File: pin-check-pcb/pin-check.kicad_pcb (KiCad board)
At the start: 2 copper layers, 76.2 x 53.3 mm, 59 parts, among them J1 AVR-ISP-6, J2 SJ-43514, P1 USB_C_Receptacle_USB2.0, SW1 MX-NoLED, SW2 MX-NoLED, SW3 MX-NoLED, SW4 MX-NoLED, SW7 Reset, SW8 Boot, U1 ATmega328P-PU, Y1 16MHz

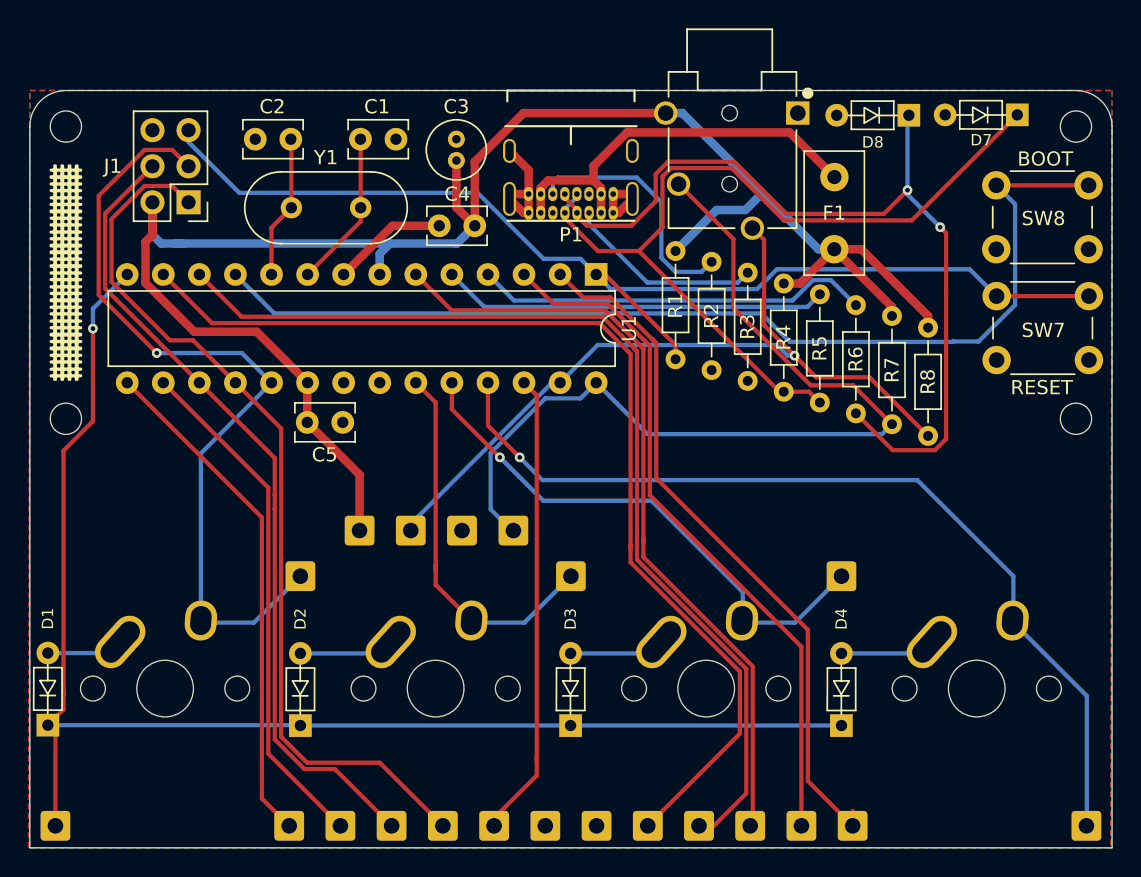
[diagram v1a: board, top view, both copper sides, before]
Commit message: buttons on top
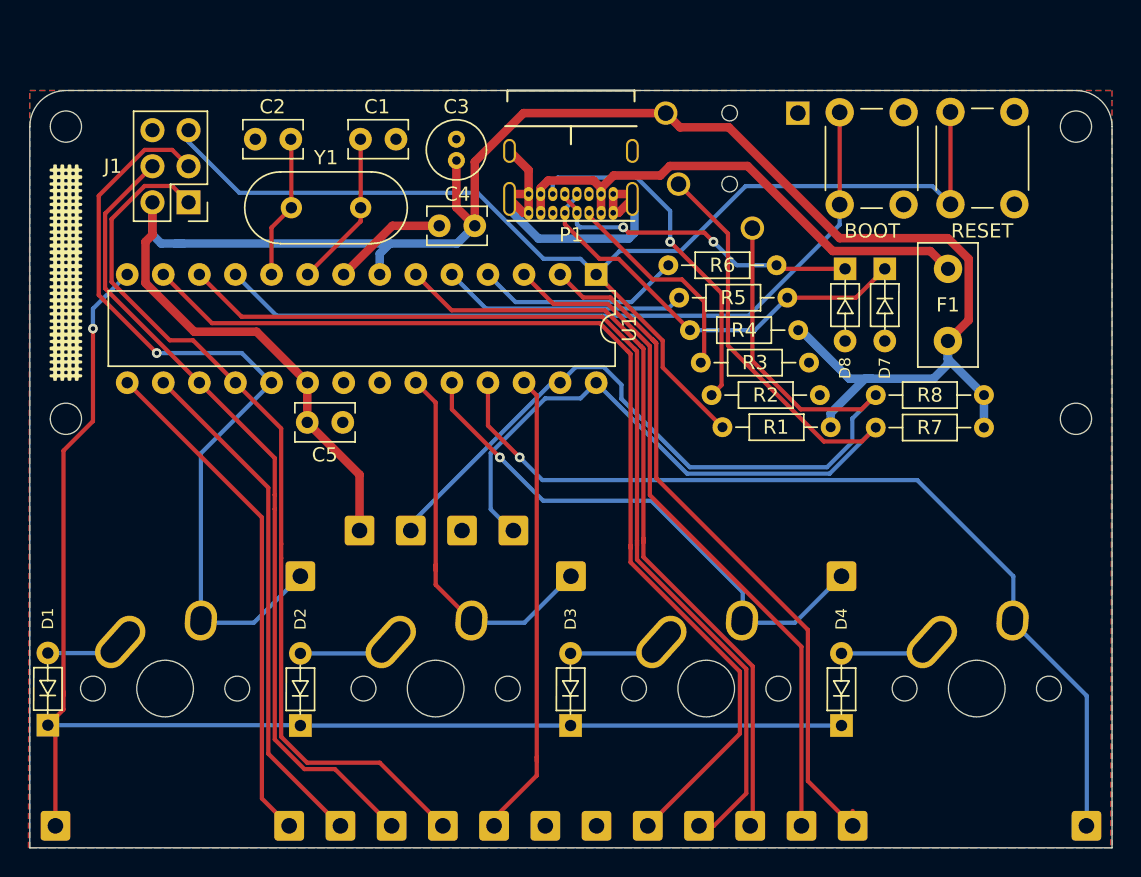
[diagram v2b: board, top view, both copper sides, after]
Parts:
- moved R1 16.5 mm to (167.2, 88.1), turned to 180 degrees
- moved D7 14.3 mm to (171.0, 75.7), turned to 270 degrees
- moved R6 11.8 mm to (163.4, 76.7), turned to 180 degrees
- moved D8 11.1 mm to (168.2, 75.7), turned to 270 degrees
- moved SW8 11.1 mm to (167.8, 72.4), turned to 90 degrees
- moved F1 10.3 mm to (175.4, 82.0)
- moved R7 10.2 mm to (178.0, 88.1), turned to 180 degrees
- moved R5 9.91 mm to (156.5, 79.0), turned to 0 degrees
- moved R2 9.38 mm to (158.8, 85.8), turned to 0 degrees
- moved SW7 7.24 mm to (175.6, 72.4), turned to 90 degrees
- moved R3 7.14 mm to (158.0, 83.5), turned to 0 degrees
- moved R8 6.17 mm to (178.0, 85.8), turned to 180 degrees
- moved R4 3.44 mm to (164.9, 81.2), turned to 180 degrees
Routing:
- net Net-(D8-Pad1): track 63.4 -> 22.9 mm
- net Net-(D7-Pad1): track 61.9 -> 30.2 mm
- net /Boot: track 73.7 -> 54.6 mm
- net GND: track 20.9 -> 35.8 mm
- net +5V: track 128.4 -> 142.5 mm
- net /D+: track 28.0 -> 14.6 mm
- net /D-: track 27.2 -> 17.3 mm
- net /SDA: track 54.9 -> 63.6 mm, vias 1 -> 0
- net Net-(F1-Pad2): track 28.5 -> 36.7 mm
- net Net-(P1-PadB5): track 17.5 -> 24.9 mm, vias 0 -> 1
- net /Reset: track 79.4 -> 83.9 mm
- net /SCL: track 63.1 -> 65.7 mm
- net Net-(P1-PadA5): track 14.5 -> 15.8 mm

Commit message: some changes
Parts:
- removed the H18 at (134.0, 95.3)
- added H22: Pad, Connector_Wire:SolderWire-0.5sqmm_1x01_D0.9mm_OD2.1mm, B.Cu at (182.9, 95.3)
- added H9: Pad, Connector_Wire:SolderWire-0.5sqmm_1x01_D0.9mm_OD2.1mm, B.Cu at (157.9, 116.1)
- moved H19 34.5 mm to (172.1, 95.3)
- moved H20 34.5 mm to (175.7, 95.3)
- moved H21 34.5 mm to (179.3, 95.3)
- moved H10 3.61 mm to (154.3, 116.1)
- moved H11 3.61 mm to (150.7, 116.1)
- moved H12 3.61 mm to (147.1, 116.1)
- moved H14 3.61 mm to (139.9, 116.1)
- moved H15 3.61 mm to (136.3, 116.1)
- moved H18 3.61 mm to (125.4, 116.1)
- moved H13 3.61 mm to (143.5, 116.1)
- moved H16 3.61 mm to (132.7, 116.1)
- moved H17 3.61 mm to (129.1, 116.1)
- renumbered H9 to H10, H10 to H11, H11 to H12, H12 to H13, H13 to H14, H14 to H15, H15 to H16, H16 to H17, H17 to H18, H22 to H23, H23 to H24, H24 to H25, H25 to H26
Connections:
- net /Boot renamed /D5
- H19 pad 1: /SDA -> /SCL
- H21 pad 1: /SCL -> /SDA
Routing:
- net /D5: track 54.6 -> 123.6 mm
- net /SCL: track 65.7 -> 58.1 mm
- net /D7: track 74.8 -> 69.0 mm
- net /D6: track 72.3 -> 67.2 mm
- net /ColD: track 65.4 -> 61.3 mm, vias 1 -> 0
- net /B4: track 63.2 -> 59.6 mm
- net /B3: track 57.4 -> 54.7 mm
- net /B2: track 36.4 -> 34.9 mm
- net +5V: track 142.5 -> 143.6 mm
- net /SDA: track 63.6 -> 62.9 mm
- net /ColC: track 38.4 -> 37.8 mm, vias 1 -> 0
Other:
- board text added: "D5"
- board text added: "pin-check v2.0.0"
- board text removed: "pin-check v1.1.0"

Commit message: 6x20
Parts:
- removed the H19 at (172.1, 95.3)
- removed the H20 at (175.7, 95.3)
- removed the H21 at (179.3, 95.3)
- removed the H22 at (182.9, 95.3)
- added J3: Conn_01x04, Connector_PinSocket_2.54mm:PinSocket_1x04_P2.54mm_Vertical, B.Cu at (181.3, 115.8)
- renumbered H23 to H19, H24 to H20, H25 to H21, H26 to H22
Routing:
- net /D1: track 49.2 -> 96.5 mm
- net +5V: track 143.6 -> 165.9 mm
- net /SCL: track 58.1 -> 80.0 mm
- net /SDA: track 62.9 -> 83.9 mm
